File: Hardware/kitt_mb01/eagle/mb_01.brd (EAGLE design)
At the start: 160 x 100 mm, 124 parts, among them IC2.0 BQ24266RGET, IC3.01 LSM9DS1, U1 MIC5205-3.3YM5TR, U1.01 RT8293A, U6.01 TPS61032RSARPSDO-G16, U7.01 SI1922EDH, U7.03 SI1922EDH, U7.2 SI1922EDH, X2.01 S2B-PH-K-S(LF)(SN), X7.02 ARDUINO_UNO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

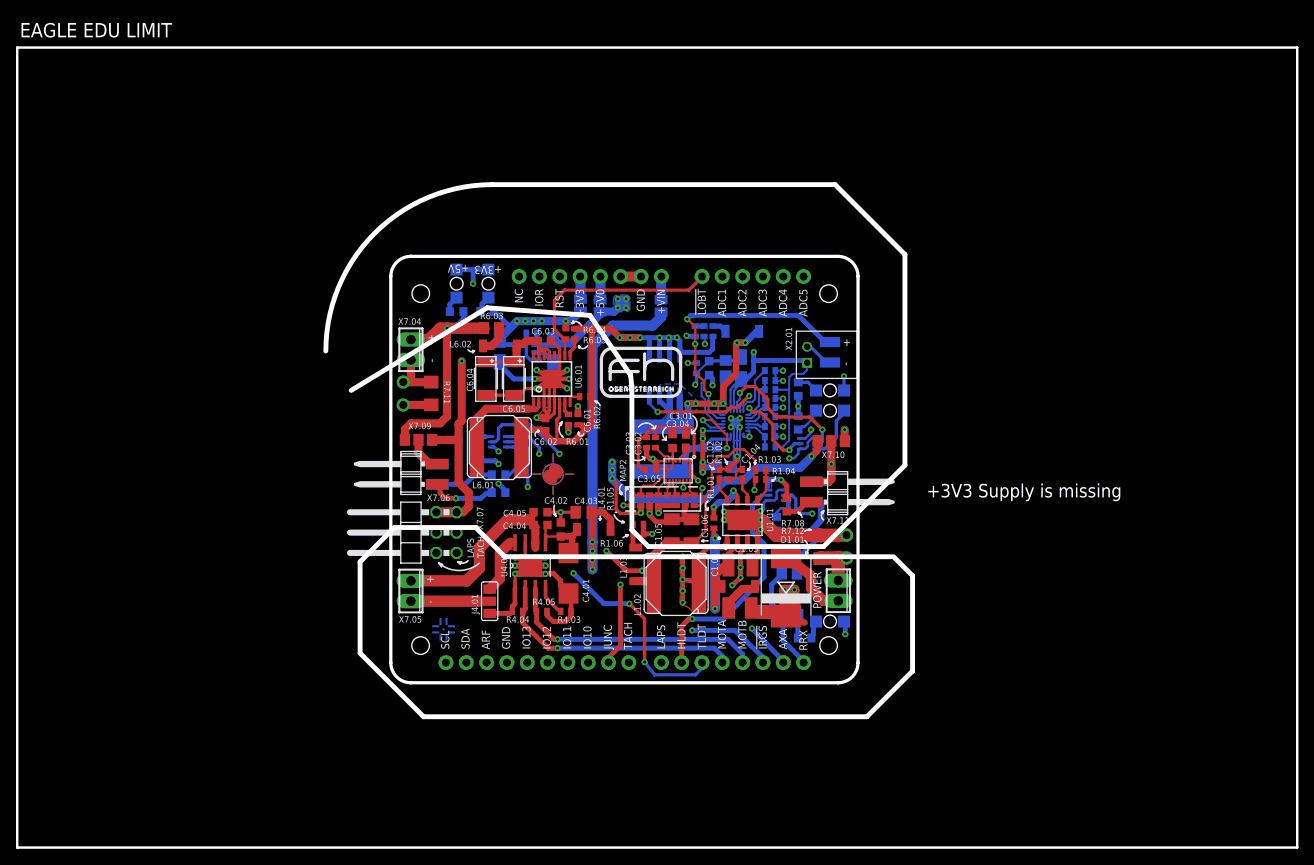
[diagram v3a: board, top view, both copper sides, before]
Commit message: snapshot of mb01 board layout -> added power plane splits (seems not ideal) -> finished slilk screening for component names -> one reroute for a lone out-of-place 3V3 wire
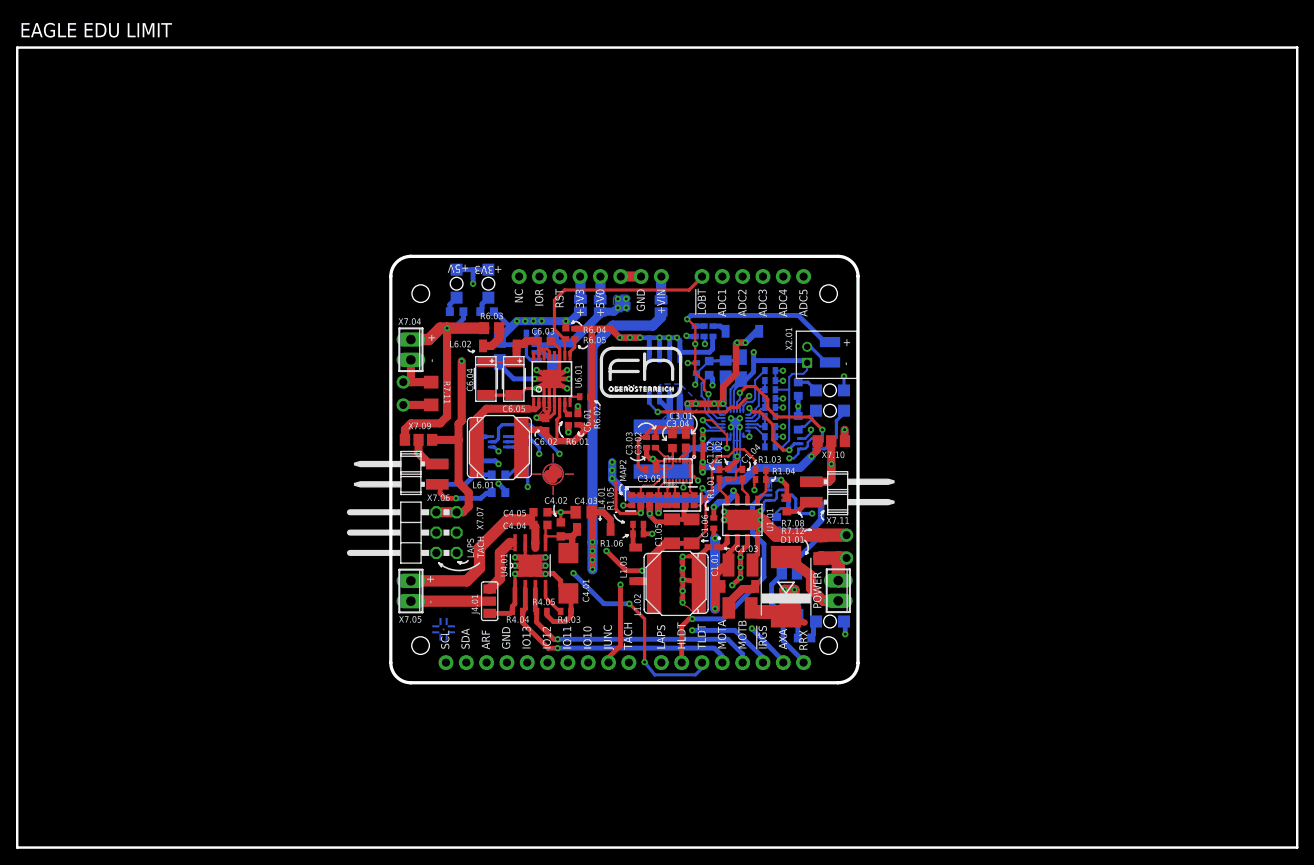
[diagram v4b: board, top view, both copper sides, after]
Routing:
- net +3V3: track 166.0 -> 159.2 mm
- net CAR.SPEED: track 30.4 -> 29.0 mm
- net N$31: track 13.9 -> 13.1 mm
- net !IRQ_GYRO: track 40.5 -> 41.2 mm
- added copper zone on layer 3, net +12V
- added copper zone on layer 3, net +3V3
- added copper zone on layer 3, net +4.1V
- added copper zone on layer 3, net GND
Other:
- outline, holes or cut-outs redrawn
- board text removed: "+3V3 Supply is missing"

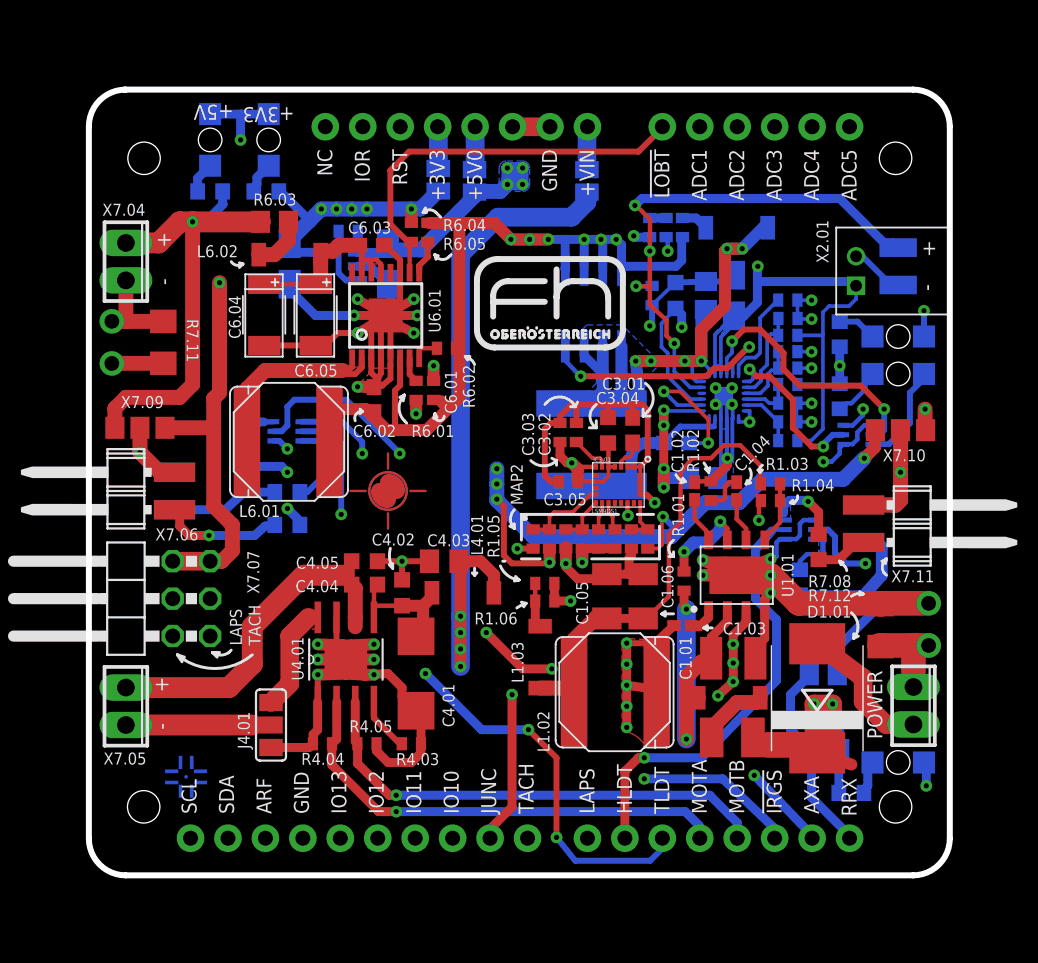
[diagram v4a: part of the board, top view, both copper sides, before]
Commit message: board layout has reached version 1.0, fresh out of alpha -> added ground stitches
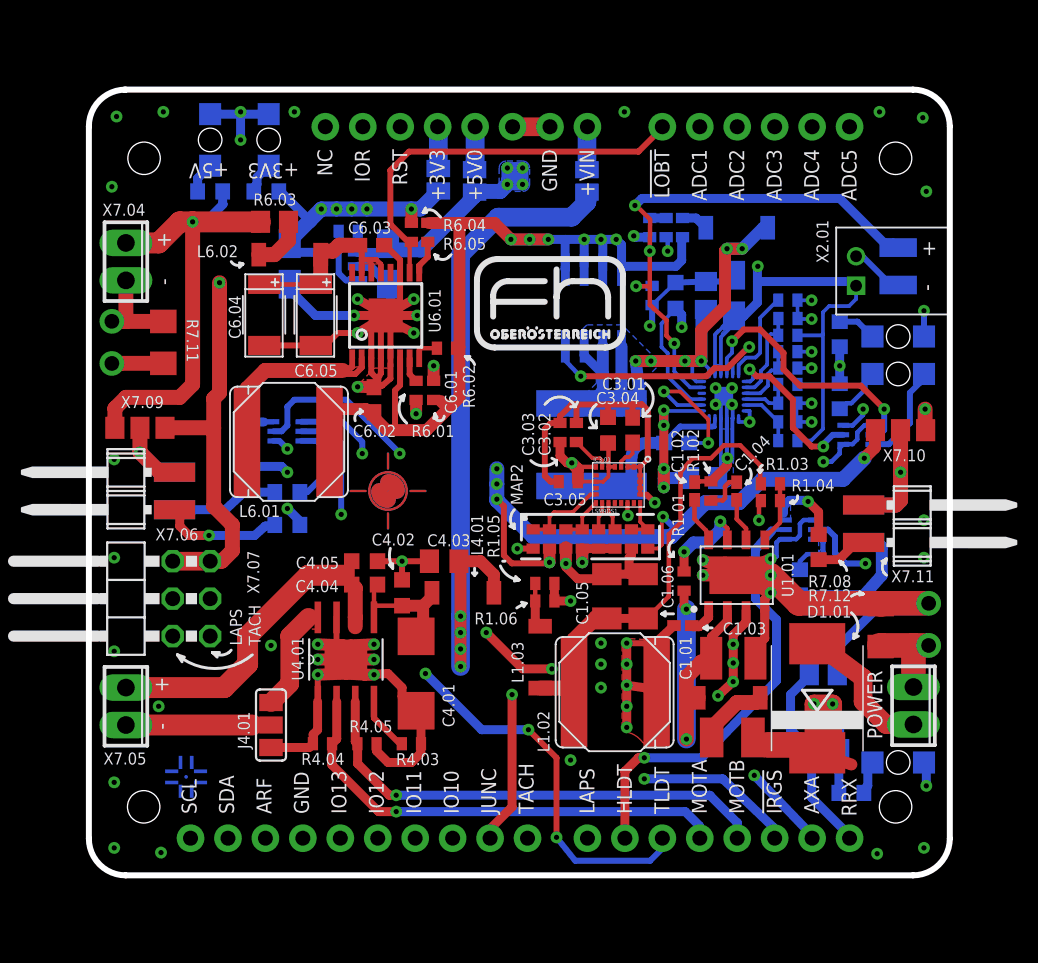
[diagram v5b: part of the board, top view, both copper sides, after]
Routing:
- net GND: vias 44 -> 69
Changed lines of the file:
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@@
 <setting verticaltext="up"/>
 </settings>
-<grid distance="3.125" unitdist="mil" unit="mil" style="lines" multiple="1" display="yes" altdistance="0.0125" altunitdist="inch" altunit="inch"/>
+<grid distance="6.25" unitdist="mil" unit="mil" style="lines" multiple="1" display="yes" altdistance="0.0125" altunitdist="inch" altunit="inch"/>
 <layers>
 <layer number="1" name="Top" color="4" fill="1" visible="yes" active="yes"/>
@@
 <wire x1="46.7" y1="71.4" x2="46.7" y2="23.1" width="0.4064" layer="20"/>
 <hole x="54.9275" y="70.485" drill="1.6"/>
-<text x="56.515" y="72.86625" size="1.016" layer="25" font="vector" rot="SR180">+5V</text>
+<text x="56.1975" y="68.8975" size="1.016" layer="25" font="vector" rot="SR180">+5V</text>
 <hole x="58.89625" y="70.485" drill="1.6"/>
-<text x="60.6425" y="72.7075" size="1.016" layer="25" font="vector" rot="SR180">+3V3</text>
+<text x="60.96" y="68.8975" size="1.016" layer="25" font="vector" rot="SR180">+3V3</text>
 <hole x="101.6" y="57.15" drill="1.6"/>
 <hole x="101.6" y="54.61" drill="1.6"/>
@@
 </element>
 <element name="D7.05" library="led" package="CHIPLED_1206" value="OK+5V" x="54.9275" y="70.485" smashed="yes" rot="MR0">
-<attribute name="NAME" x="52.613125" y="68.976875" size="0.8128" layer="26" font="vector" rot="MR90"/>
+<attribute name="NAME" x="52.613125" y="68.500625" size="0.8128" layer="26" font="vector" rot="MR90"/>
 </element>
 <element name="R7.13" library="rcl" package="R0603" value="330R" x="54.9275" y="66.9925" smashed="yes" rot="MR180">
@@
 </element>
 <element name="D7.06" library="led" package="CHIPLED_1206" value="OK+3V" x="58.89625" y="70.485" smashed="yes" rot="MR0">
-<attribute name="NAME" x="60.3125" y="68.976875" size="0.8128" layer="26" font="vector" rot="MR90"/>
+<attribute name="NAME" x="60.15375" y="68.500625" size="0.8128" layer="26" font="vector" rot="MR90"/>
 </element>
 <element name="R7.14" library="rcl" package="R0603" value="330R" x="58.7375" y="66.9925" smashed="yes" rot="MR180">
@@
 <vertex x="80.9625" y="42.2275" curve="125.087804"/>
 </polygon>
-<wire x1="92.948125" y1="39.766875" x2="93.0275" y2="39.84625" width="0" layer="19" extent="1-1"/>
-<wire x1="62.215" y1="32.385" x2="62.23" y2="32.385" width="0" layer="19" extent="1-1"/>
+<polygon width="0.6096" layer="1" rank="6">
+<vertex x="46.6725" y="71.4375"/>
+<vertex x="46.6725" y="23.1775" curve="90"/>
+<vertex x="49.2125" y="20.6375"/>
+<vertex x="102.5525" y="20.6375" curve="90"/>
+<vertex x="105.0925" y="23.1775"/>
+<vertex x="105.0925" y="71.4375" curve="90"/>
+<vertex x="102.5525" y="73.9775"/>
+<vertex x="49.2125" y="73.9775" curve="90"/>
+</polygon>
+<polygon width="0.6096" layer="16" rank="6">
+<vertex x="49.2125" y="73.9775" curve="90"/>
+<vertex x="46.6725" y="71.4375"/>
+<vertex x="46.6725" y="23.1775" curve="90"/>
+<vertex x="49.2125" y="20.6375"/>
+<vertex x="102.5525" y="20.6375" curve="90"/>
+<vertex x="105.0925" y="23.1775"/>
+<vertex x="105.0925" y="71.4375" curve="90"/>
+<vertex x="102.5525" y="73.9775"/>
+</polygon>
+<via x="48.26" y="67.31" extent="1-16" drill="0.35"/>
+<via x="48.5775" y="72.0725" extent="1-16" drill="0.35"/>
+<via x="51.7525" y="72.39" extent="1-16" drill="0.35"/>
+<via x="60.6425" y="72.39" extent="1-16" drill="0.35"/>
+<via x="83.02625" y="72.39" extent="1-16" drill="0.35"/>
+<via x="103.34625" y="42.148125" extent="1-16" drill="0.35"/>
+<via x="103.266875" y="71.993125" extent="1-16" drill="0.35"/>
+<via x="100.33" y="72.39" extent="1-16" drill="0.35"/>
+<via x="103.505" y="66.9925" extent="1-16" drill="0.35"/>
+<via x="103.34625" y="44.688125" extent="1-16" drill="0.35"/>
+<via x="103.34625" y="22.463125" extent="1-16" drill="0.35"/>
+<via x="48.41875" y="22.463125" extent="1-16" drill="0.35"/>
+<via x="51.59375" y="22.145625" extent="1-16" drill="0.35"/>
+<via x="48.41875" y="26.908125" extent="1-16" drill="0.35"/>
+<via x="48.41875" y="35.798125" extent="1-16" drill="0.35"/>
+<via x="48.41875" y="48.815625" extent="1-16" drill="0.35"/>
+<via x="48.41875" y="42.148125" extent="1-16" drill="0.35"/>
+<via x="56.99125" y="72.39" extent="1-16" drill="0.35"/>
+<via x="51.435" y="32.0675" extent="1-16" drill="0.35"/>
+<via x="59.055" y="36.195" extent="1-16" drill="0.35"/>
+<via x="81.43875" y="36.35375" extent="1-16" drill="0.35"/>
+<via x="81.43875" y="34.925" extent="1-16" drill="0.35"/>
+<via x="81.43875" y="33.3375" extent="1-16" drill="0.35"/>
+<via x="79.375" y="28.41625" extent="1-16" drill="0.35"/>
+<via x="100.17125" y="22.06625" extent="1-16" drill="0.35"/>
 </signal>
 <signal name="+12V">
@@
 <wire x1="74.13625" y1="34.76625" x2="76.99375" y2="39.21125" width="0.6096" layer="3" curve="-11.382615"/>
 <wire x1="76.99375" y1="39.21125" x2="78.184375" y2="40.3225" width="0.6096" layer="3" curve="-30.925292"/>
-<wire x1="83.5025" y1="27.225625" x2="82.629375" y2="27.225625" width="0.6096" layer="3"/>
-<wire x1="82.629375" y1="27.225625" x2="78.4225" y2="30.1625" width="0.6096" layer="3" curve="-90"/>
-<wire x1="78.4225" y1="30.1625" x2="77.47" y2="32.0675" width="0.6096" layer="3" curve="90"/>
+<wire x1="83.5025" y1="27.225625" x2="82.470625" y2="27.384375" width="0.6096" layer="3"/>
+<wire x1="82.470625" y1="27.384375" x2="80.3275" y2="30.1625" width="0.6096" layer="3" curve="-90"/>
+<wire x1="80.3275" y1="30.1625" x2="77.47" y2="32.0675" width="0.6096" layer="3" curve="90"/>
 <wire x1="77.47" y1="32.0675" x2="76.2" y2="31.75" width="0.6096" layer="3" curve="53.130102"/>
 <wire x1="75.644375" y1="31.59125" x2="76.2" y2="31.75" width="0.6096" layer="3" curve="3.431471"/>
@@
 <wire x1="64.53" y1="41.91" x2="64.53" y2="40.3225" width="0.4064" layer="1"/>
 <wire x1="64.8475" y1="40.3225" x2="64.53" y2="40.3225" width="0.4064" layer="1"/>
-<wire x1="49.2125" y1="33.3375" x2="56.1975" y2="33.3375" width="1.4224" layer="1"/>
-<wire x1="56.1975" y1="33.3375" x2="57.785" y2="34.925" width="1.4224" layer="1"/>
-<wire x1="57.785" y1="34.925" x2="57.785" y2="37.465" width="1.4224" layer="1"/>
-<wire x1="57.785" y1="37.465" x2="61.2775" y2="40.9575" width="1.4224" layer="1"/>
-<wire x1="61.2775" y1="40.9575" x2="63.97625" y2="40.9575" width="1.4224" layer="1"/>
+<wire x1="49.2125" y1="33.3375" x2="55.88" y2="33.3375" width="1.4224" layer="1"/>
+<wire x1="55.88" y1="33.3375" x2="57.4675" y2="34.925" width="1.4224" layer="1"/>
+<wire x1="57.4675" y1="34.925" x2="57.4675" y2="36.83" width="1.4224" layer="1"/>
+<wire x1="57.4675" y1="36.83" x2="61.595" y2="40.9575" width="1.4224" layer="1"/>
+<wire x1="61.595" y1="40.9575" x2="63.97625" y2="40.9575" width="1.4224" layer="1"/>
 <wire x1="63.97625" y1="40.9575" x2="64.53" y2="40.40375" width="0.4064" layer="1"/>
 <wire x1="64.53" y1="40.40375" x2="64.53" y2="40.3225" width="0.4064" layer="1"/>
@@
 <wire x1="91.836875" y1="27.384375" x2="88.9" y2="28.41625" width="0.6096" layer="3" curve="90"/>
 <wire x1="88.9" y1="28.41625" x2="85.328125" y2="28.971875" width="0.6096" layer="3" curve="-87.617023"/>
-<wire x1="85.328125" y1="28.971875" x2="83.5025" y2="28.8925" width="0.6096" layer="3" curve="126.40107"/>
-<wire x1="83.5025" y1="28.8925" x2="82.470625" y2="28.495625" width="0.6096" layer="3" curve="-57.383905"/>
+<wire x1="85.328125" y1="28.971875" x2="83.34375" y2="29.05125" width="0.6096" layer="3" curve="126.40107"/>
+<wire x1="83.34375" y1="29.05125" x2="82.470625" y2="28.813125" width="0.6096" layer="3" curve="-57.383905"/>
 <via x="78.105" y="34.6075" extent="1-16" drill="0.35"/>
 <wire x1="78.105" y1="34.6075" x2="76.120625" y2="34.6075" width="0.6096" layer="1"/>
 <wire x1="76.120625" y1="34.6075" x2="73.66" y2="37.068125" width="0.6096" layer="1"/>
-<wire x1="81.28" y1="29.5275" x2="82.311875" y2="28.495625" width="0.6096" layer="3" curve="90"/>
-<wire x1="82.311875" y1="28.495625" x2="82.470625" y2="28.495625" width="0.6096" layer="3"/>
-<wire x1="81.28" y1="29.5275" x2="78.105" y2="34.6075" width="0.6096" layer="3" curve="64.010766"/>
+<wire x1="81.43875" y1="29.68625" x2="82.311875" y2="28.813125" width="0.6096" layer="3" curve="90"/>
+<wire x1="82.311875" y1="28.813125" x2="82.470625" y2="28.813125" width="0.6096" layer="3"/>
+<wire x1="81.43875" y1="29.68625" x2="78.105" y2="34.6075" width="0.6096" layer="3" curve="64.010766"/>
 </signal>
 <signal name="N$49">
